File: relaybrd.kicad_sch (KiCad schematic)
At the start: 1 part, among them J7 5499922-4

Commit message: push from windows
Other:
- moved on the sheet: J7

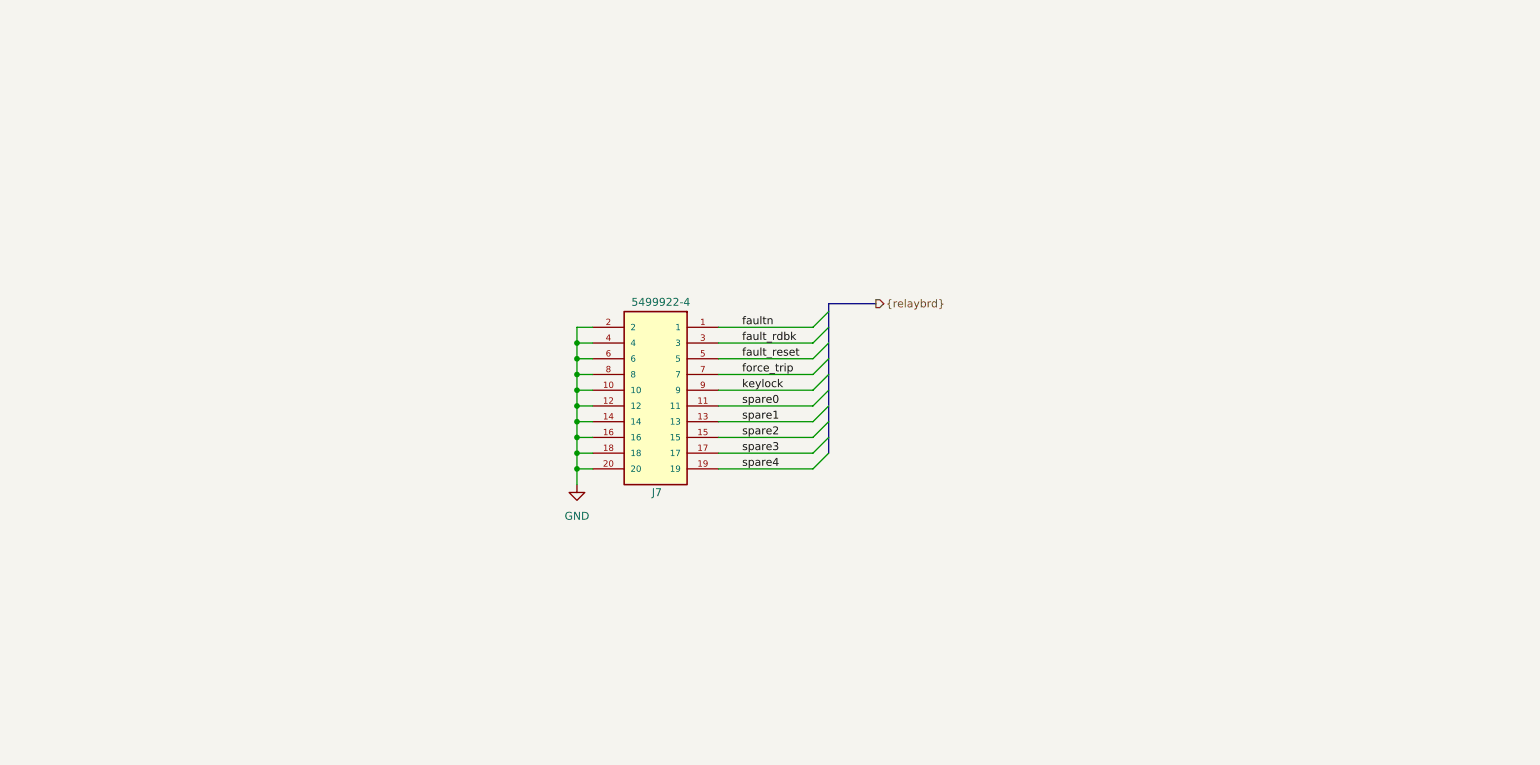
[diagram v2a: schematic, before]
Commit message: Add watchdog window IC
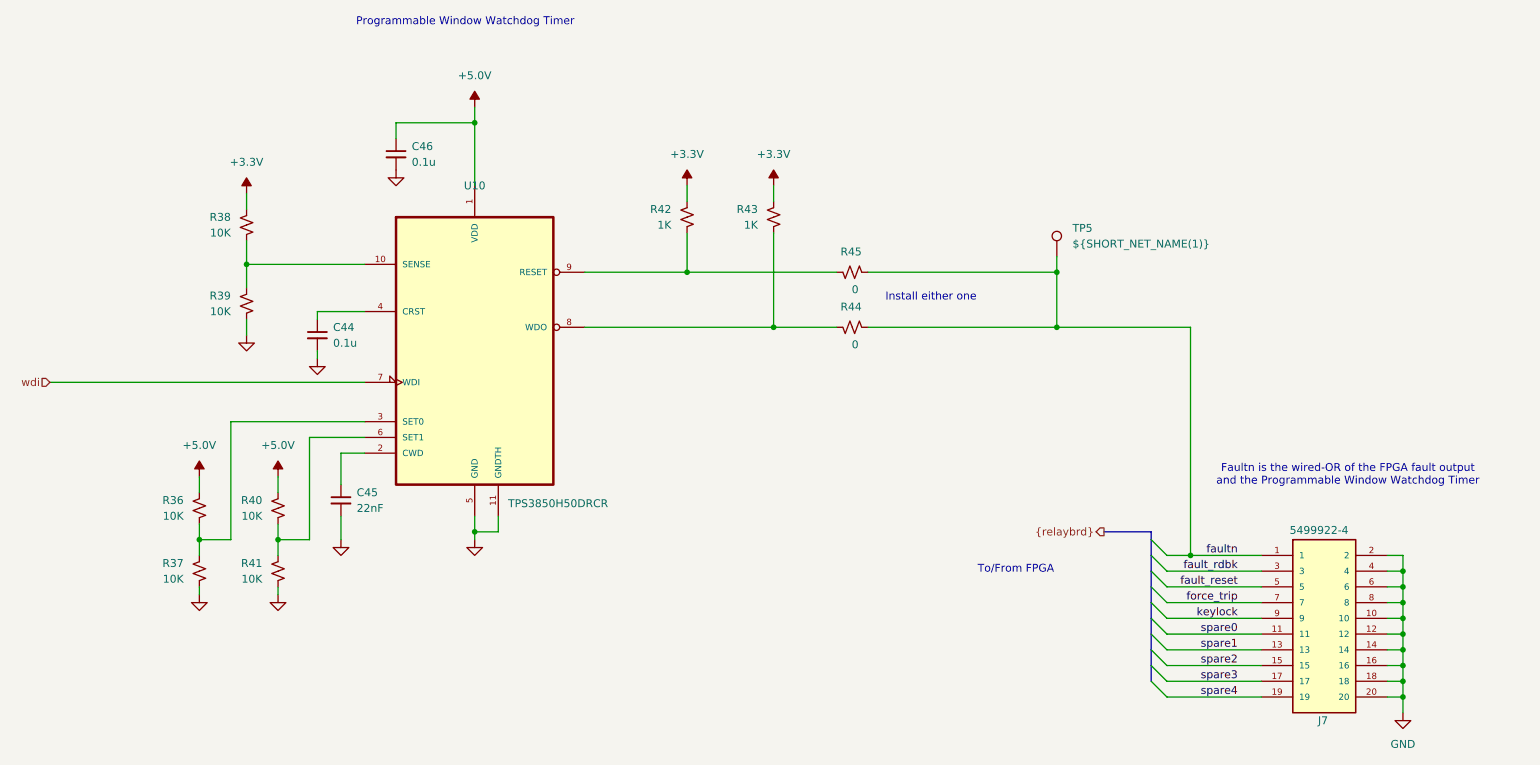
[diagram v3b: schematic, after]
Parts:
- added C44, C46: 0.1u, Capacitor_SMD:C_0805_2012Metric, symbol Device:C_Small
- added C45: 22nF, Capacitor_SMD:C_0805_2012Metric, symbol Device:C_Small
- added R36, R37, R38, R39, R40, R41: 10K, Resistor_SMD:R_0805_2012Metric, symbol Device:R_Small_US
- added R42, R43: 1K, Resistor_SMD:R_0805_2012Metric, symbol Device:R_Small_US
- added R44, R45: 0, Resistor_SMD:R_0805_2012Metric, symbol Device:R_Small_US
- added TP5: ${SHORT_NET_NAME(1)}, My Footprints:TestPoint_RCS-0C, symbol Connector:TestPoint
- added U10: TPS3850H50DRCR, My Footprints:TPS3850_DRCR, symbol My Symbols:TPS3850H50DRCR
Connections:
- net GND: now also C44.2, C45.2, C46.2, R37.2, R39.2, R41.2, U10.11 (GNDTH), U10.5 (GND)
- net faultn: now also R44.2, R45.2, TP5.1
- new net: C45.1, U10.2 (CWD)
- new net: R42.2, R45.1, U10.9 (RESET)
- new net: R43.2, R44.1, U10.8 (WDO)
- new net: R36.2, R37.1, U10.3 (SET0)
- new net: R40.2, R41.1, U10.6 (SET1)
- new net: R38.2, R39.1, U10.10 (SENSE)
- new net: C44.1, U10.4 (CRST)
- new net +3.3V: R38.1, R42.1, R43.1
- new net +5.0V: C46.1, R36.1, R40.1, U10.1 (VDD)
- new net wdi: U10.7 (WDI)
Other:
- note added: "Faultn is the wired-OR of the FPGA fault output and the Programmable Window Watchdog Timer"
- note added: "Install either one"
- note added: "Programmable Window Watchdog Timer"
- note added: "To/From FPGA"
- moved on the sheet: J7

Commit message: Finish BOM
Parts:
- C44, C46: Cost (none) -> .08; MFG (none) -> Taiyo-Yuden; MFG_PN (none) -> TMF212B7104KGHT
- C45: Cost (none) -> .15; MFG (none) -> Kemet; MFG_PN (none) -> C0805C223J3GEC7210
- J7: Cost (none) -> 5.00; MFG (none) -> Molex; MFG_PN (none) -> 5499922-4
- R42, R43: MFG_PN ERJ-2RKF1001X -> ERJ-P06F1001V
- U10: Cost (none) -> 1.85; MFG (none) -> TI

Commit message: Nightly commit
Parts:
- C44, C45, C46: footprint Capacitor_SMD:C_0805_2012Metric -> My Footprints:C_0805_2012Metric
- TP5: value ${SHORT_NET_NAME(1)} -> faultn
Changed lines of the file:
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@@
 			)
 		)
-		(property "Value" "${SHORT_NET_NAME(1)}"
+		(property "Value" "faultn"
 			(at 208.28 71.6279 0)
 			(effects
@@
 			)
 		)
-		(property "Footprint" "Capacitor_SMD:C_0805_2012Metric"
+		(property "Footprint" "My Footprints:C_0805_2012Metric"
 			(at 90.17 113.03 0)
 			(effects
@@
 			)
 		)
-		(property "Footprint" "Capacitor_SMD:C_0805_2012Metric"
+		(property "Footprint" "My Footprints:C_0805_2012Metric"
 			(at 86.36 86.36 0)
 			(effects
@@
 			)
 		)
-		(property "Footprint" "Capacitor_SMD:C_0805_2012Metric"
+		(property "Footprint" "My Footprints:C_0805_2012Metric"
 			(at 99.06 57.15 0)
 			(effects
